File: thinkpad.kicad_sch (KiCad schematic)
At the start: 125 parts, among them J1 Conn_01x06_MountingPin, J2 Conn_01x20_Socket, J3 Conn_01x06_Socket, SW1 SW_Push, U1 Raspberry_Pi_Pico

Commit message: Fix gnd
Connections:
- net GND: now also J1.MP (MountPin)
- no-connect marks 5 -> 4
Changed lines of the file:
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@@
   )
   (no_connect (at 50.8 119.38))
-  (no_connect (at 54.61 153.67))
   (no_connect (at 39.37 138.43))
   (no_connect (at 50.8 116.84))
@@
     )
   )
+  (global_label "GND" (shape input) (at 54.61 153.67 270) (fields_autoplaced)
+    (effects (font (size 1.27 1.27)) (justify right))
+    (property "Intersheetrefs" "${INTERSHEET_REFS}" (at 54.61 160.5257 90)
+      (effects (font (size 1.27 1.27)) (justify right) hide)
+    )
+  )

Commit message: Improvements
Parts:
- added JP1: SolderJumper_3_Open, Jumper:SolderJumper-3_P1.3mm_Open_Pad1.0x1.5mm_NumberLabels, symbol Jumper:SolderJumper_3_Open
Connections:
- net Col 0: now also U1.16 (GPIO12); no longer U1.15 (GPIO11)
- net Col 1: now also U1.15 (GPIO11); no longer U1.14 (GPIO10)
- net Col 2: now also U1.14 (GPIO10); no longer U1.13 (GND)
- net GND: now also JP1.1 (A)
- net SC_DTCT: now also JP1.2 (C)
- net VCC: now also JP1.3 (B)

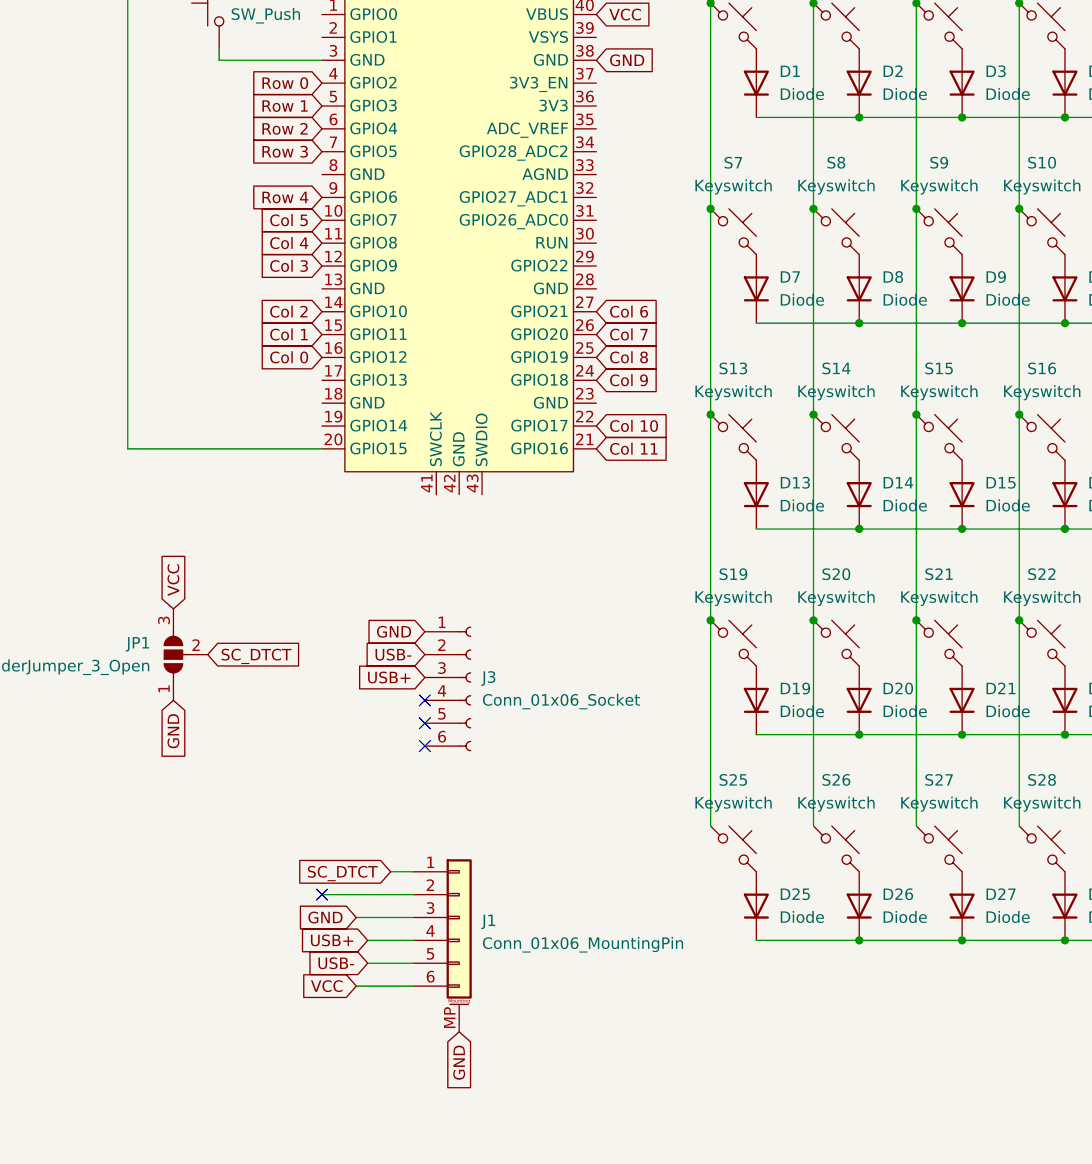
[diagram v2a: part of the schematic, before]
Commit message: Made space for touchpad, fixed connection of cols, added pads for touchpad i2c
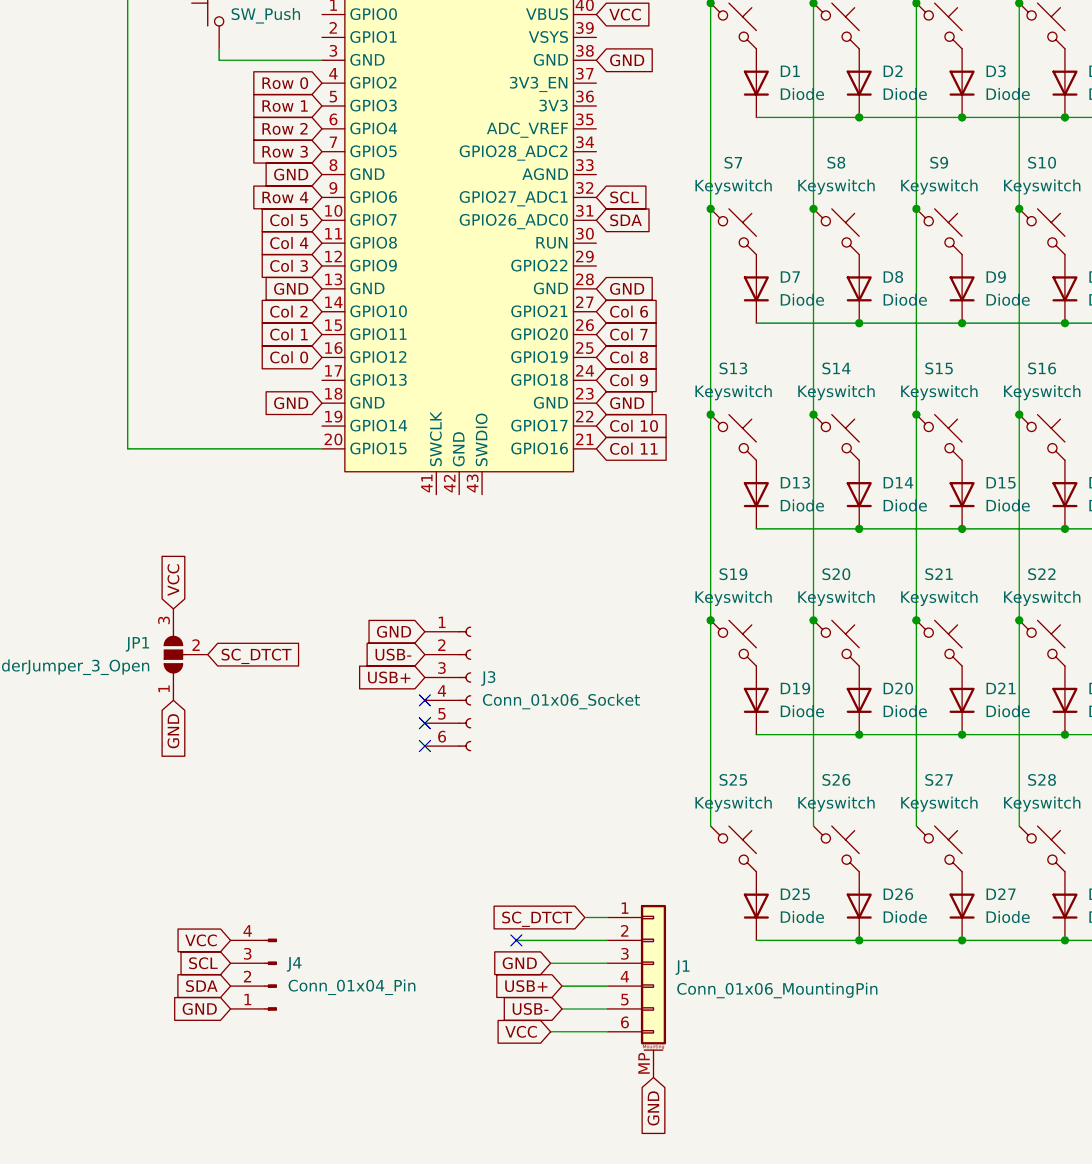
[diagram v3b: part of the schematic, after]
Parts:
- added J4: Conn_01x04_Pin, Connector_PinHeader_2.54mm:PinHeader_1x04_P2.54mm_Vertical, symbol Connector:Conn_01x04_Pin
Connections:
- net GND: now also U1.13 (GND), U1.18 (GND), U1.23 (GND), U1.28 (GND), U1.8 (GND), J4.1 (Pin_1)
- net VCC: now also J4.4 (Pin_4)
- net SDA: now reaches U1.31 (GPIO26_ADC0)
- net SDA: now also J4.2 (Pin_2)
- net SCL: now reaches U1.32 (GPIO27_ADC1)
- net SCL: now also J4.3 (Pin_3)
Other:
- moved on the sheet: J1

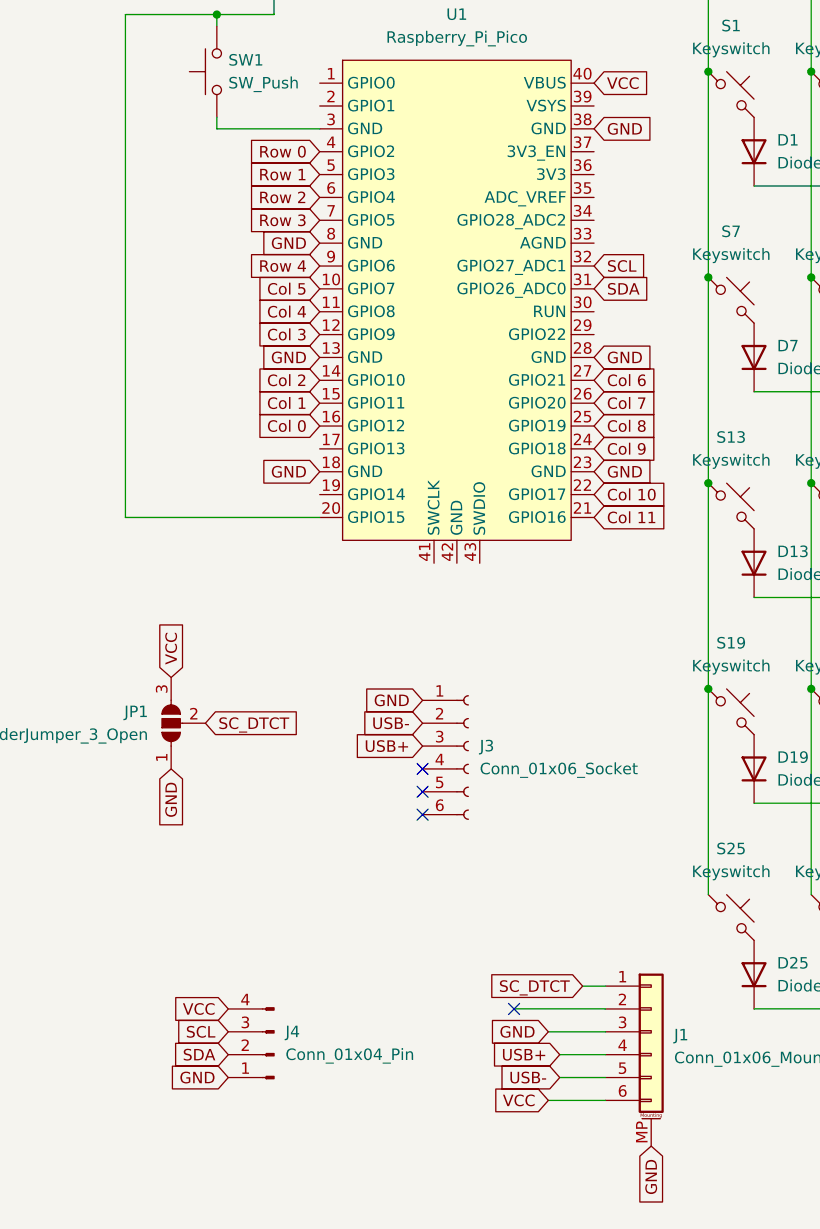
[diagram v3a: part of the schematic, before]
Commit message: Give 3V3 to touchpad
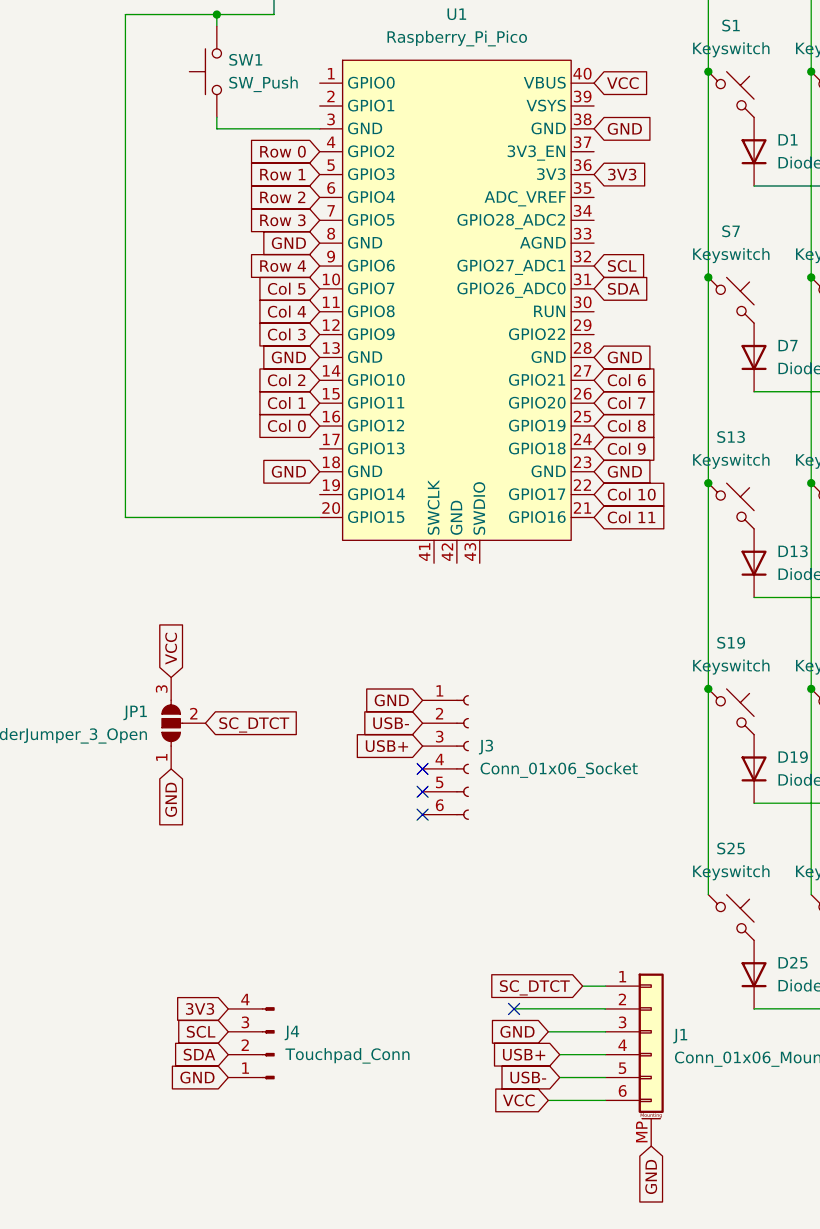
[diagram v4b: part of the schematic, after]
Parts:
- J4: value Conn_01x04_Pin -> Touchpad_Conn
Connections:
- net VCC: no longer J4.4 (Pin_4)
- net 3V3: now reaches U1.36 (3V3)
- net 3V3: now also J4.4 (Pin_4)
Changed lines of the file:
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@@
-    )
-  )
-  (global_label "VCC" (shape input) (at 29.21 143.51 180) (fields_autoplaced)
-    (effects (font (size 1.27 1.27)) (justify right))
-    (property "Intersheetrefs" "${INTERSHEET_REFS}" (at 22.5962 143.51 0)
-      (effects (font (size 1.27 1.27)) (justify right) hide)
     )
   )
@@
     )
   )
+  (global_label "3V3" (shape input) (at 69.85 50.8 0) (fields_autoplaced)
+    (effects (font (size 1.27 1.27)) (justify left))
+    (property "Intersheetrefs" "${INTERSHEET_REFS}" (at 76.3428 50.8 0)
+      (effects (font (size 1.27 1.27)) (justify left) hide)
+    )
+  )
   (global_label "Row 0" (shape input) (at 252.73 52.07 0) (fields_autoplaced)
     (effects (font (size 1.27 1.27)) (justify left))
@@
     (property "Intersheetrefs" "${INTERSHEET_REFS}" (at 212.09 18.4235 90)
       (effects (font (size 1.27 1.27)) (justify left) hide)
+    )
+  )
+  (global_label "3V3" (shape input) (at 29.21 143.51 180) (fields_autoplaced)
+    (effects (font (size 1.27 1.27)) (justify right))
+    (property "Intersheetrefs" "${INTERSHEET_REFS}" (at 22.7172 143.51 0)
+      (effects (font (size 1.27 1.27)) (justify right) hide)
     )
   )
@@
       (effects (font (size 1.27 1.27)) (justify right))
     )
-    (property "Value" "Conn_01x04_Pin" (at 35.56 148.59 0)
-      (effects (font (size 1.27 1.27)) (justify right))
-    )
+    (property "Value" "Touchpad_Conn" (at 35.56 148.59 0)
+      (effects (font (size 1.27 1.27)) (justify right))
+    )

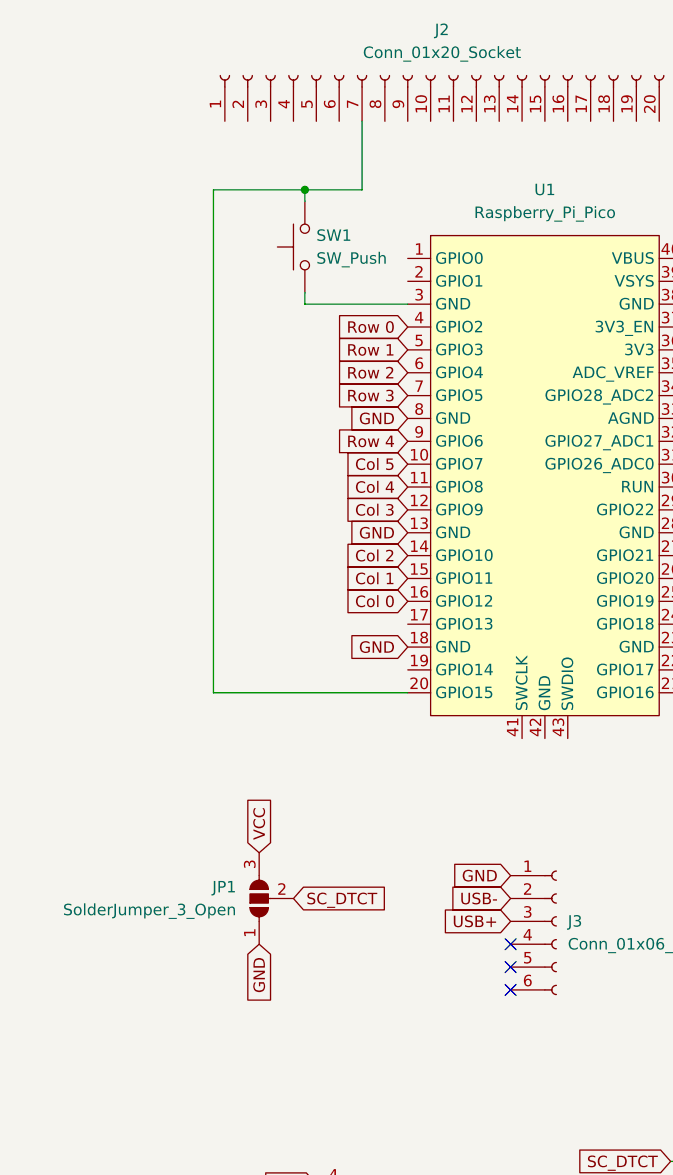
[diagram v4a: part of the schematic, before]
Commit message: Fix issue with usb and aligning the tape
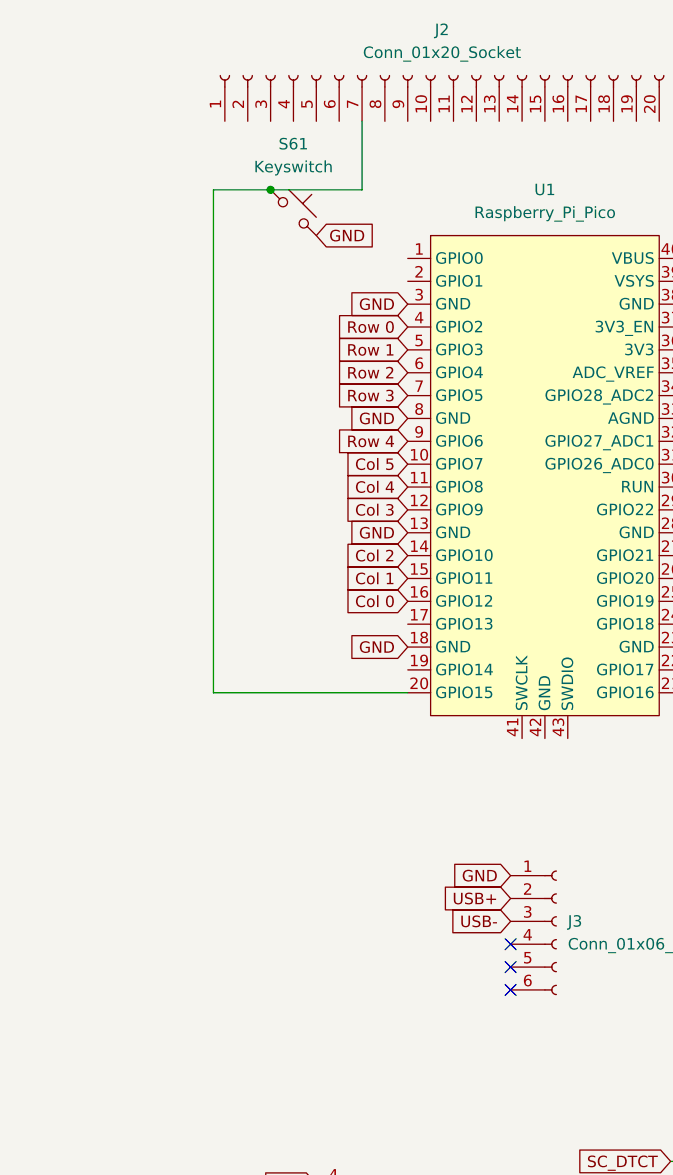
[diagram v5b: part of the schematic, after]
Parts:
- removed JP1: SolderJumper_3_Open, Jumper:SolderJumper-3_P1.3mm_Open_Pad1.0x1.5mm_NumberLabels, symbol Jumper:SolderJumper_3_Open
- removed SW1: SW_Push, Button_Switch_THT:SW_PUSH-12mm, symbol Switch:SW_Push
- added S61: Keyswitch, ScottoKeebs_Choc:Choc_Mini_1.00u, symbol ScottoKeebs:Placeholder_Keyswitch
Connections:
- net GND: now also U1.3 (GND), S61.2
- net USB+: now also J3.2 (Pin_2); no longer J3.3 (Pin_3)
- net USB-: now also J3.3 (Pin_3); no longer J3.2 (Pin_2)
- net at J2.7 (Pin_7), U1.20 (GPIO15): now also S61.1
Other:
- company: (none) -> VerdandiTeam
- title: (none) -> Thinkpad keybaord

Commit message: Change switches
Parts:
- added F1: Fuse, Fuse:Fuse_0805_2012Metric, symbol Device:Fuse
- added J5: Alt_USB, Connector_PinHeader_2.54mm:PinHeader_1x04_P2.54mm_Vertical, symbol Connector:Conn_01x04_Pin
- added JP1: PowerPin_Jumper_Reverse, Jumper:SolderJumper-2_P1.3mm_Open_Pad1.0x1.5mm, symbol Jumper:SolderJumper_2_Open
- added JP2: PowerPin_Jumper, Jumper:SolderJumper-2_P1.3mm_Open_Pad1.0x1.5mm, symbol Jumper:SolderJumper_2_Open
- D1, D10, D11, D12, D13, D14, D15, D16, D17, D18, D19, D2, D20, D21, D22, D23, D24, D25, D26, D27, D28, D29, D3, D30, D31, D32, D33, D34, D35, D36, D37, D38, D39, D4, D40, D41, D42, D43, D44, D45, D46, D47, D48, D49, D5, D50, D51, D52, D53, D54, D55, D56, D57, D58, D59, D6, D60, D7, D8, D9: footprint ScottoKeebs_Components:Diode_DO-35 -> thinkpad-keyboard:Diode_SMD_THT2
- S1, S10, S11, S12, S13, S14, S15, S16, S17, S18, S19, S2, S20, S21, S22, S23, S24, S25, S26, S27, S28, S29, S3, S30, S31, S32, S33, S34, S35, S36, S37, S38, S39, S4, S40, S41, S42, S43, S44, S45, S46, S47, S48, S49, S5, S50, S51, S52, S53, S54, S55, S56, S57, S58, S59, S6, S60, S61, S7, S8, S9: footprint ScottoKeebs_Choc:Choc_Mini_1.00u -> kailh-pg1425-x-switch:Kailh-PG1425-X-Switch
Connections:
- net GND: now also J1.4 (Pin_4), J1.6 (Pin_6), J5.1 (Pin_1); no longer J1.3 (Pin_3)
- net USB+: now also J1.3 (Pin_3), J5.2 (Pin_2); no longer J1.4 (Pin_4)
- net USB-: now also J1.2 (Pin_2), J5.3 (Pin_3); no longer J1.5 (Pin_5)
- net VCC: now also F1.2, J5.4 (Pin_4); no longer J1.6 (Pin_6)
- net at S61.1, U1.20 (GPIO15): now also JP1.1 (A), JP2.1 (A); no longer J2.7 (Pin_7)
- net at J2.14 (Pin_14): now also JP1.2 (B)
- net SC_DTCT: no longer names the net of J1.1 (Pin_1)
- net SC_DTCT: now also F1.1
- new net: J2.7 (Pin_7), JP2.2 (B)
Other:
- moved on the sheet: S61, U1
